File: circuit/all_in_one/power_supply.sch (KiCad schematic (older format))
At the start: 23 parts

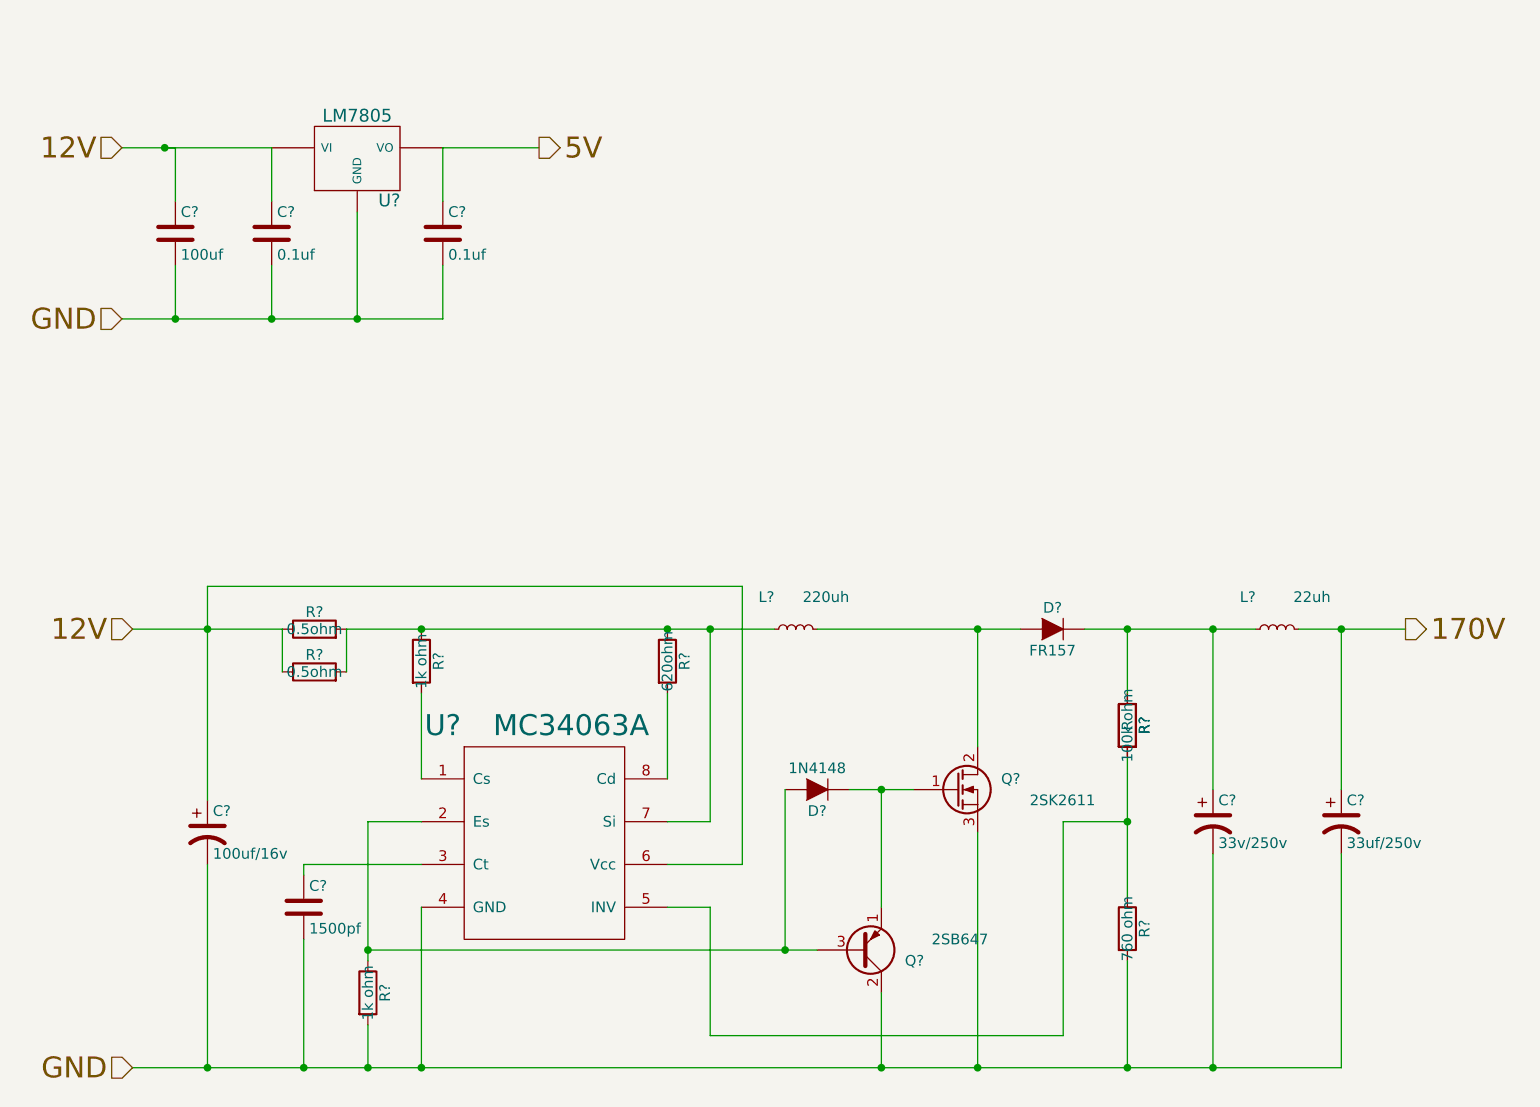
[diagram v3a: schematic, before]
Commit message: [All in one]Define part of compoment's footprint
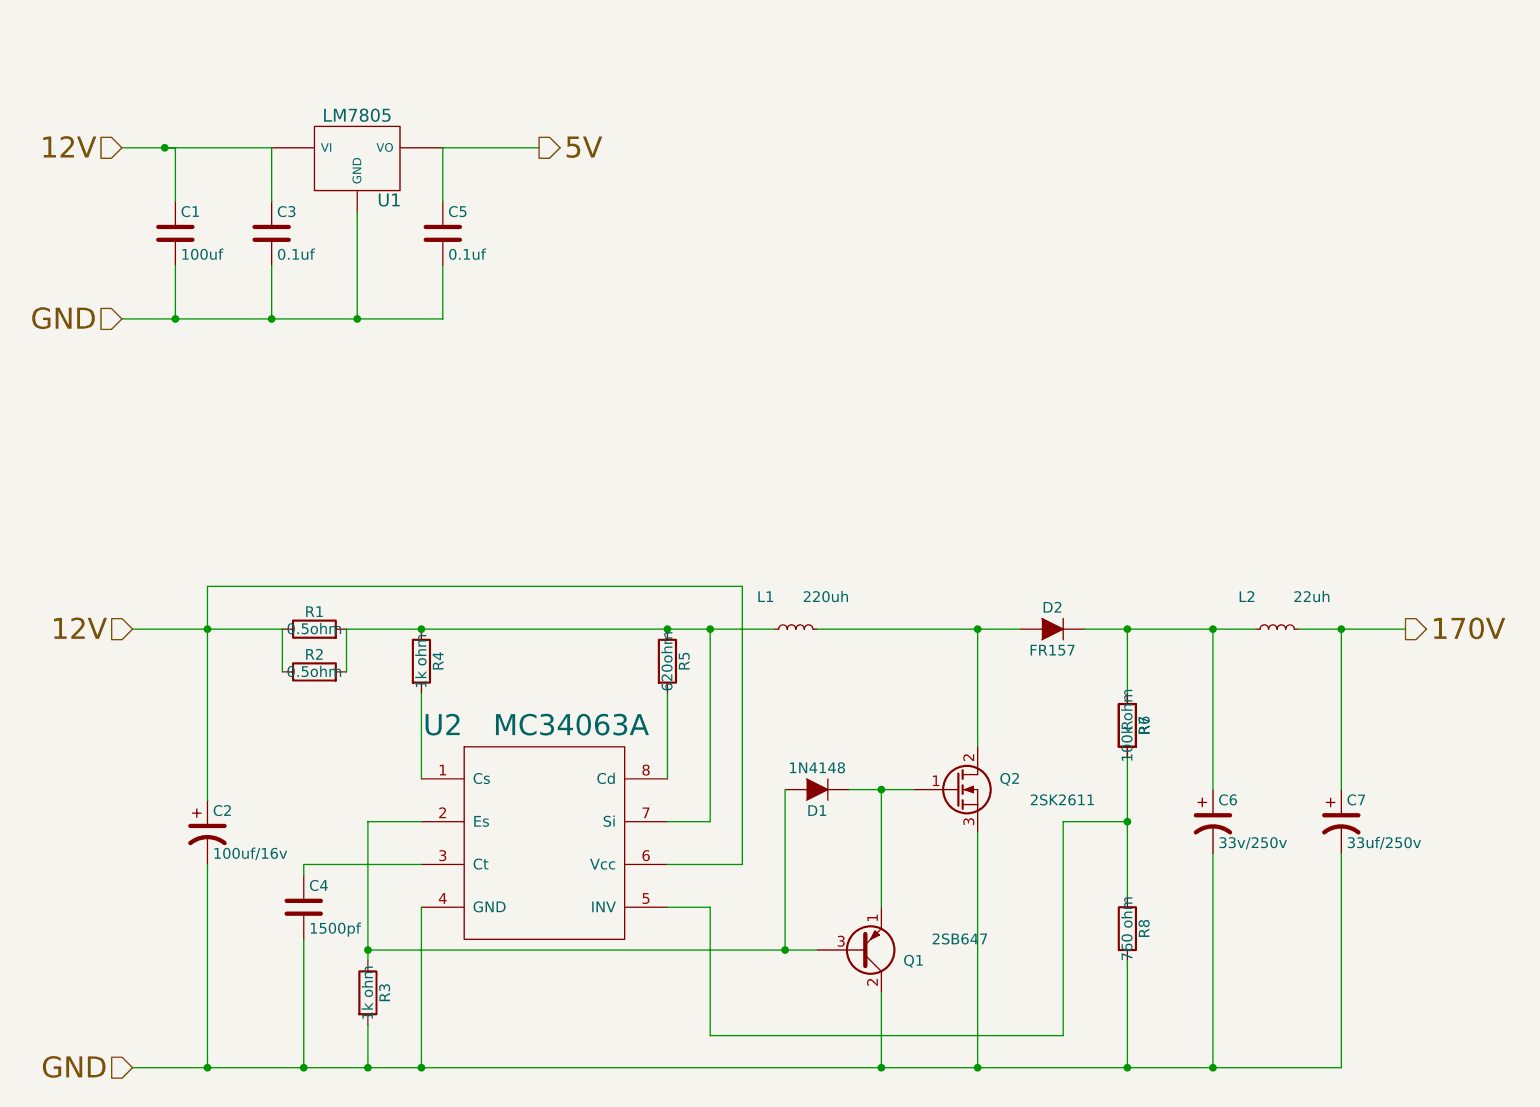
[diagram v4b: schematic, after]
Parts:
- U1: renamed from U?; footprint (none) -> Transistors_SMD:sot404
- U2: renamed from U?; footprint (none) -> Power_Integrations:SO-8
- gave numbers to parts that had none: 21
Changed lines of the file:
@@
 GND
 $Comp
-L LM7805 U?
+L LM7805 U1
 U 1 1 56462C05
 P 3600 1750
-F 0 "U?" H 3750 1554 60  0000 C CNN
+F 0 "U1" H 3750 1554 60  0000 C CNN
 F 1 "LM7805" H 3600 1950 60  0000 C CNN
-F 2 "" H 3600 1750 60  0000 C CNN
+F 2 "Transistors_SMD:sot404" H 3600 1750 60  0001 C CNN
 F 3 "" H 3600 1750 60  0000 C CNN
 	1    3600 1750
@@
 $EndComp
 $Comp
-L C C?
+L C C1
 U 1 1 56462C7B
 P 2750 2100
-F 0 "C?" H 2775 2200 50  0000 L CNN
+F 0 "C1" H 2775 2200 50  0000 L CNN
 F 1 "100uf" H 2775 2000 50  0000 L CNN
-F 2 "" H 2788 1950 30  0000 C CNN
+F 2 "" H 2788 1950 30  0001 C CNN
 F 3 "" H 2750 2100 60  0000 C CNN
 	1    2750 2100
@@
 $EndComp
 $Comp
-L C C?
+L C C3
 U 1 1 56462D16
 P 3200 2100
-F 0 "C?" H 3225 2200 50  0000 L CNN
+F 0 "C3" H 3225 2200 50  0000 L CNN
 F 1 "0.1uf" H 3225 2000 50  0000 L CNN
-F 2 "" H 3238 1950 30  0000 C CNN
+F 2 "" H 3238 1950 30  0001 C CNN
 F 3 "" H 3200 2100 60  0000 C CNN
 	1    3200 2100
@@
 $EndComp
 $Comp
-L C C?
+L C C5
 U 1 1 56462D5B
 P 4000 2100
-F 0 "C?" H 4025 2200 50  0000 L CNN
+F 0 "C5" H 4025 2200 50  0000 L CNN
 F 1 "0.1uf" H 4025 2000 50  0000 L CNN
-F 2 "" H 4038 1950 30  0000 C CNN
+F 2 "" H 4038 1950 30  0001 C CNN
 F 3 "" H 4000 2100 60  0000 C CNN
 	1    4000 2100
@@
 Connection ~ 2700 1700
 $Comp
-L MC34063A U?
+L MC34063A U2
 U 1 1 564633D2
 P 4500 5000
-F 0 "U?" H 4000 5600 98  0000 C CNN
+F 0 "U2" H 4000 5600 98  0000 C CNN
 F 1 "MC34063A" H 4600 5600 98  0000 C CNN
-F 2 "" H 4500 5600 98  0000 C CNN
+F 2 "Power_Integrations:SO-8" H 4500 5600 98  0001 C CNN
 F 3 "" H 4500 5600 98  0000 C CNN
 	1    4500 5000
@@
 $EndComp
 $Comp
-L C C?
+L C C4
 U 1 1 5646359C
 P 3350 5250
-F 0 "C?" H 3375 5350 50  0000 L CNN
+F 0 "C4" H 3375 5350 50  0000 L CNN
 F 1 "1500pf" H 3375 5150 50  0000 L CNN
-F 2 "" H 3388 5100 30  0000 C CNN
+F 2 "" H 3388 5100 30  0001 C CNN
 F 3 "" H 3350 5250 60  0000 C CNN
 	1    3350 5250
@@
 $EndComp
 $Comp
-L R R?
+L R R1
 U 1 1 56463665
 P 3400 3950
-F 0 "R?" V 3480 3950 50  0000 C CNN
+F 0 "R1" V 3480 3950 50  0000 C CNN
 F 1 "0.5ohm" V 3400 3950 50  0000 C CNN
-F 2 "" V 3330 3950 30  0000 C CNN
+F 2 "" V 3330 3950 30  0001 C CNN
 F 3 "" H 3400 3950 30  0000 C CNN
 	1    3400 3950
@@
 $EndComp
 $Comp
-L R R?
+L R R2
 U 1 1 564636F4
 P 3400 4150
-F 0 "R?" V 3480 4150 50  0000 C CNN
+F 0 "R2" V 3480 4150 50  0000 C CNN
 F 1 "0.5ohm" V 3400 4150 50  0000 C CNN
-F 2 "" V 3330 4150 30  0000 C CNN
+F 2 "" V 3330 4150 30  0001 C CNN
 F 3 "" H 3400 4150 30  0000 C CNN
 	1    3400 4150
@@
 $EndComp
 $Comp
-L R R?
+L R R4
 U 1 1 56463737
 P 3900 4100
-F 0 "R?" V 3980 4100 50  0000 C CNN
+F 0 "R4" V 3980 4100 50  0000 C CNN
 F 1 "1k ohm" V 3900 4100 50  0000 C CNN
-F 2 "" V 3830 4100 30  0000 C CNN
+F 2 "" V 3830 4100 30  0001 C CNN
 F 3 "" H 3900 4100 30  0000 C CNN
 	1    3900 4100
@@
 $EndComp
 $Comp
-L R R?
+L R R5
 U 1 1 56463766
 P 5050 4100
-F 0 "R?" V 5130 4100 50  0000 C CNN
+F 0 "R5" V 5130 4100 50  0000 C CNN
 F 1 "620ohm" V 5050 4100 50  0000 C CNN
-F 2 "" V 4980 4100 30  0000 C CNN
+F 2 "" V 4980 4100 30  0001 C CNN
 F 3 "" H 5050 4100 30  0000 C CNN
 	1    5050 4100
@@
 $EndComp
 $Comp
-L CP1 C?
+L CP1 C2
 U 1 1 564637A1
 P 2900 4900
-F 0 "C?" H 2925 5000 50  0000 L CNN
+F 0 "C2" H 2925 5000 50  0000 L CNN
 F 1 "100uf/16v" H 2925 4800 50  0000 L CNN
-F 2 "" H 2900 4900 60  0000 C CNN
+F 2 "" H 2900 4900 60  0001 C CNN
 F 3 "" H 2900 4900 60  0000 C CNN
 	1    2900 4900
@@
 $EndComp
 $Comp
-L CP1 C?
+L CP1 C6
 U 1 1 56463846
 P 7600 4850
-F 0 "C?" H 7625 4950 50  0000 L CNN
+F 0 "C6" H 7625 4950 50  0000 L CNN
 F 1 "33v/250v" H 7625 4750 50  0000 L CNN
-F 2 "" H 7600 4850 60  0000 C CNN
+F 2 "" H 7600 4850 60  0001 C CNN
 F 3 "" H 7600 4850 60  0000 C CNN
 	1    7600 4850
@@
 $EndComp
 $Comp
-L CP1 C?
+L CP1 C7
 U 1 1 5646389B
 P 8200 4850
-F 0 "C?" H 8225 4950 50  0000 L CNN
+F 0 "C7" H 8225 4950 50  0000 L CNN
 F 1 "33uf/250v" H 8225 4750 50  0000 L CNN
-F 2 "" H 8200 4850 60  0000 C CNN
+F 2 "" H 8200 4850 60  0001 C CNN
 F 3 "" H 8200 4850 60  0000 C CNN
 	1    8200 4850
@@
 $EndComp
 $Comp
-L R R?
+L R R6
 U 1 1 56463908
 P 7200 4400
-F 0 "R?" V 7280 4400 50  0000 C CNN
+F 0 "R6" V 7280 4400 50  0000 C CNN
 F 1 "100k ohm" V 7200 4400 50  0000 C CNN
-F 2 "" V 7130 4400 30  0000 C CNN
+F 2 "" V 7130 4400 30  0001 C CNN
 F 3 "" H 7200 4400 30  0000 C CNN
 	1    7200 4400
@@
 $EndComp
 $Comp
-L R R?
+L R R8
 U 1 1 56463951
 P 7200 5350
-F 0 "R?" V 7280 5350 50  0000 C CNN
+F 0 "R8" V 7280 5350 50  0000 C CNN
 F 1 "760 ohm" V 7200 5350 50  0000 C CNN
-F 2 "" V 7130 5350 30  0000 C CNN
+F 2 "" V 7130 5350 30  0001 C CNN
 F 3 "" H 7200 5350 30  0000 C CNN
 	1    7200 5350
@@
 $EndComp
 $Comp
-L D D?
+L D D2
 U 1 1 56463990
 P 6850 3950
-F 0 "D?" H 6850 4050 50  0000 C CNN
+F 0 "D2" H 6850 4050 50  0000 C CNN
 F 1 "FR157" H 6850 3850 50  0000 C CNN
-F 2 "" H 6850 3950 60  0000 C CNN
+F 2 "" H 6850 3950 60  0001 C CNN
 F 3 "" H 6850 3950 60  0000 C CNN
 	1    6850 3950
@@
 $EndComp
 $Comp
-L D D?
+L D D1
 U 1 1 564639E5
 P 5750 4700
-F 0 "D?" H 5750 4800 50  0000 C CNN
+F 0 "D1" H 5750 4800 50  0000 C CNN
 F 1 "1N4148" H 5750 4600 50  0000 C CNN
-F 2 "" H 5750 4700 60  0000 C CNN
+F 2 "" H 5750 4700 60  0001 C CNN
 F 3 "" H 5750 4700 60  0000 C CNN
 	1    5750 4700
@@
 	3900 5250 3900 6000
 $Comp
-L R R?
+L R R3
 U 1 1 5646515D
 P 3650 5650
-F 0 "R?" V 3730 5650 50  0000 C CNN
+F 0 "R3" V 3730 5650 50  0000 C CNN
 F 1 "1k ohm" V 3650 5650 50  0000 C CNN
-F 2 "" V 3580 5650 30  0000 C CNN
+F 2 "" V 3580 5650 30  0001 C CNN
 F 3 "" H 3650 5650 30  0000 C CNN
 	1    3650 5650
@@
 	3350 5050 3900 5050
 $Comp
-L L_Small L?
+L L_Small L1
 U 1 1 564660D5
 P 5650 3950
-F 0 "L?" V 5800 4050 50  0000 L CNN
+F 0 "L1" V 5800 4050 50  0000 L CNN
 F 1 "220uh" V 5800 3700 50  0000 L CNN
-F 2 "" H 5650 3950 60  0000 C CNN
+F 2 "" H 5650 3950 60  0001 C CNN
 F 3 "" H 5650 3950 60  0000 C CNN
 	1    5650 3950
@@
 $EndComp
 $Comp
-L L_Small L?
+L L_Small L2
 U 1 1 56466786
 P 7900 3950
-F 0 "L?" V 8050 4050 50  0000 L CNN
+F 0 "L2" V 8050 4050 50  0000 L CNN
 F 1 "22uh" V 8050 3700 50  0000 L CNN
-F 2 "" H 7900 3950 60  0000 C CNN
+F 2 "" H 7900 3950 60  0001 C CNN
 F 3 "" H 7900 3950 60  0000 C CNN
 	1    7900 3950
@@
 Connection ~ 5250 3950
 $Comp
-L Q_PNP_ECB Q?
+L Q_PNP_ECB Q1
 U 1 1 56466938
 P 5950 5450
-F 0 "Q?" H 6250 5500 50  0000 R CNN
+F 0 "Q1" H 6250 5500 50  0000 R CNN
 F 1 "2SB647" H 6550 5400 50  0000 R CNN
-F 2 "" H 6150 5550 29  0000 C CNN
+F 2 "" H 6150 5550 29  0001 C CNN
 F 3 "" H 5950 5450 60  0000 C CNN
 	1    5950 5450
@@
 $EndComp
 $Comp
-L Q_NMOS_GDS Q?
+L Q_NMOS_GDS Q2
 U 1 1 56466AEF
 P 6400 4700
-F 0 "Q?" H 6700 4750 50  0000 R CNN
+F 0 "Q2" H 6700 4750 50  0000 R CNN
 F 1 "2SK2611" H 7050 4650 50  0000 R CNN
-F 2 "" H 6600 4800 29  0000 C CNN
+F 2 "" H 6600 4800 29  0001 C CNN
 F 3 "" H 6400 4700 60  0000 C CNN
 	1    6400 4700
@@
 Connection ~ 8200 3950
 $Comp
-L R R?
+L R R7
 U 1 1 56481750
 P 7200 4400
-F 0 "R?" V 7280 4400 50  0000 C CNN
+F 0 "R7" V 7280 4400 50  0000 C CNN
 F 1 "R" V 7200 4400 50  0000 C CNN
-F 2 "" V 7130 4400 30  0000 C CNN
+F 2 "" V 7130 4400 30  0001 C CNN
 F 3 "" H 7200 4400 30  0000 C CNN
 	1    7200 4400

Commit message: [All in one]Select resister and power jack's footprint
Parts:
- R1, R2, R3, R4, R5, R6, R7, R8: footprint (none) -> Resistors_SMD:R_0805_HandSoldering
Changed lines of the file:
@@
 F 0 "R1" V 3480 3950 50  0000 C CNN
 F 1 "0.5ohm" V 3400 3950 50  0000 C CNN
-F 2 "" V 3330 3950 30  0001 C CNN
+F 2 "Resistors_SMD:R_0805_HandSoldering" V 3330 3950 30  0001 C CNN
 F 3 "" H 3400 3950 30  0000 C CNN
 	1    3400 3950
@@
 F 0 "R2" V 3480 4150 50  0000 C CNN
 F 1 "0.5ohm" V 3400 4150 50  0000 C CNN
-F 2 "" V 3330 4150 30  0001 C CNN
+F 2 "Resistors_SMD:R_0805_HandSoldering" V 3330 4150 30  0001 C CNN
 F 3 "" H 3400 4150 30  0000 C CNN
 	1    3400 4150
@@
 F 0 "R4" V 3980 4100 50  0000 C CNN
 F 1 "1k ohm" V 3900 4100 50  0000 C CNN
-F 2 "" V 3830 4100 30  0001 C CNN
+F 2 "Resistors_SMD:R_0805_HandSoldering" V 3830 4100 30  0001 C CNN
 F 3 "" H 3900 4100 30  0000 C CNN
 	1    3900 4100
@@
 F 0 "R5" V 5130 4100 50  0000 C CNN
 F 1 "620ohm" V 5050 4100 50  0000 C CNN
-F 2 "" V 4980 4100 30  0001 C CNN
+F 2 "Resistors_SMD:R_0805_HandSoldering" V 4980 4100 30  0001 C CNN
 F 3 "" H 5050 4100 30  0000 C CNN
 	1    5050 4100
@@
 F 0 "R6" V 7280 4400 50  0000 C CNN
 F 1 "100k ohm" V 7200 4400 50  0000 C CNN
-F 2 "" V 7130 4400 30  0001 C CNN
+F 2 "Resistors_SMD:R_0805_HandSoldering" V 7130 4400 30  0001 C CNN
 F 3 "" H 7200 4400 30  0000 C CNN
 	1    7200 4400
@@
 F 0 "R8" V 7280 5350 50  0000 C CNN
 F 1 "760 ohm" V 7200 5350 50  0000 C CNN
-F 2 "" V 7130 5350 30  0001 C CNN
+F 2 "Resistors_SMD:R_0805_HandSoldering" V 7130 5350 30  0001 C CNN
 F 3 "" H 7200 5350 30  0000 C CNN
 	1    7200 5350
@@
 F 0 "R3" V 3730 5650 50  0000 C CNN
 F 1 "1k ohm" V 3650 5650 50  0000 C CNN
-F 2 "" V 3580 5650 30  0001 C CNN
+F 2 "Resistors_SMD:R_0805_HandSoldering" V 3580 5650 30  0001 C CNN
 F 3 "" H 3650 5650 30  0000 C CNN
 	1    3650 5650
@@
 F 0 "R7" V 7280 4400 50  0000 C CNN
 F 1 "R" V 7200 4400 50  0000 C CNN
-F 2 "" V 7130 4400 30  0001 C CNN
+F 2 "Resistors_SMD:R_0805_HandSoldering" V 7130 4400 30  0001 C CNN
 F 3 "" H 7200 4400 30  0000 C CNN
 	1    7200 4400

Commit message: [All in one]Select footprint for capacitors
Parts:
- C1, C2: footprint (none) -> Capacitors_Tantalum_SMD:TantalC_SizeC_EIA-6032_HandSoldering
- C3, C4, C5: footprint (none) -> Capacitors_SMD:C_0805_HandSoldering
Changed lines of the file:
@@
 F 0 "C1" H 2775 2200 50  0000 L CNN
 F 1 "100uf" H 2775 2000 50  0000 L CNN
-F 2 "" H 2788 1950 30  0001 C CNN
+F 2 "Capacitors_Tantalum_SMD:TantalC_SizeC_EIA-6032_HandSoldering" H 2788 1950 30  0001 C CNN
 F 3 "" H 2750 2100 60  0000 C CNN
 	1    2750 2100
@@
 F 0 "C3" H 3225 2200 50  0000 L CNN
 F 1 "0.1uf" H 3225 2000 50  0000 L CNN
-F 2 "" H 3238 1950 30  0001 C CNN
+F 2 "Capacitors_SMD:C_0805_HandSoldering" H 3238 1950 30  0001 C CNN
 F 3 "" H 3200 2100 60  0000 C CNN
 	1    3200 2100
@@
 F 0 "C5" H 4025 2200 50  0000 L CNN
 F 1 "0.1uf" H 4025 2000 50  0000 L CNN
-F 2 "" H 4038 1950 30  0001 C CNN
+F 2 "Capacitors_SMD:C_0805_HandSoldering" H 4038 1950 30  0001 C CNN
 F 3 "" H 4000 2100 60  0000 C CNN
 	1    4000 2100
@@
 F 0 "C4" H 3375 5350 50  0000 L CNN
 F 1 "1500pf" H 3375 5150 50  0000 L CNN
-F 2 "" H 3388 5100 30  0001 C CNN
+F 2 "Capacitors_SMD:C_0805_HandSoldering" H 3388 5100 30  0001 C CNN
 F 3 "" H 3350 5250 60  0000 C CNN
 	1    3350 5250
@@
 F 0 "C2" H 2925 5000 50  0000 L CNN
 F 1 "100uf/16v" H 2925 4800 50  0000 L CNN
-F 2 "" H 2900 4900 60  0001 C CNN
+F 2 "Capacitors_Tantalum_SMD:TantalC_SizeC_EIA-6032_HandSoldering" H 2900 4900 60  0001 C CNN
 F 3 "" H 2900 4900 60  0000 C CNN
 	1    2900 4900

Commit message: Finished select all the component footprint
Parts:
- C6, C7: footprint (none) -> Capacitors_ThroughHole:C_Radial_D13_L21_P5
- D1, D2: footprint (none) -> Diodes_ThroughHole:Diode_DO-35_SOD27_Horizontal_RM10
- L1, L2: footprint (none) -> Inductors:INDUCTOR_V
- Q1: footprint (none) -> TO_SOT_Packages_THT:TO-92_Inline_Narrow_Oval
- Q2: footprint (none) -> TO_SOT_Packages_THT:TO-220_Neutral123_PadsOnly
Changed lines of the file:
@@
 F 0 "C6" H 7625 4950 50  0000 L CNN
 F 1 "33v/250v" H 7625 4750 50  0000 L CNN
-F 2 "" H 7600 4850 60  0001 C CNN
+F 2 "Capacitors_ThroughHole:C_Radial_D13_L21_P5" H 7600 4850 60  0001 C CNN
 F 3 "" H 7600 4850 60  0000 C CNN
 	1    7600 4850
@@
 F 0 "C7" H 8225 4950 50  0000 L CNN
 F 1 "33uf/250v" H 8225 4750 50  0000 L CNN
-F 2 "" H 8200 4850 60  0001 C CNN
+F 2 "Capacitors_ThroughHole:C_Radial_D13_L21_P5" H 8200 4850 60  0001 C CNN
 F 3 "" H 8200 4850 60  0000 C CNN
 	1    8200 4850
@@
 F 0 "D2" H 6850 4050 50  0000 C CNN
 F 1 "FR157" H 6850 3850 50  0000 C CNN
-F 2 "" H 6850 3950 60  0001 C CNN
+F 2 "Diodes_ThroughHole:Diode_DO-35_SOD27_Horizontal_RM10" H 6850 3950 60  0001 C CNN
 F 3 "" H 6850 3950 60  0000 C CNN
 	1    6850 3950
@@
 F 0 "D1" H 5750 4800 50  0000 C CNN
 F 1 "1N4148" H 5750 4600 50  0000 C CNN
-F 2 "" H 5750 4700 60  0001 C CNN
+F 2 "Diodes_ThroughHole:Diode_DO-35_SOD27_Horizontal_RM10" H 5750 4700 60  0001 C CNN
 F 3 "" H 5750 4700 60  0000 C CNN
 	1    5750 4700
@@
 F 0 "L1" V 5800 4050 50  0000 L CNN
 F 1 "220uh" V 5800 3700 50  0000 L CNN
-F 2 "" H 5650 3950 60  0001 C CNN
+F 2 "Inductors:INDUCTOR_V" H 5650 3950 60  0001 C CNN
 F 3 "" H 5650 3950 60  0000 C CNN
 	1    5650 3950
@@
 F 0 "L2" V 8050 4050 50  0000 L CNN
 F 1 "22uh" V 8050 3700 50  0000 L CNN
-F 2 "" H 7900 3950 60  0001 C CNN
+F 2 "Inductors:INDUCTOR_V" H 7900 3950 60  0001 C CNN
 F 3 "" H 7900 3950 60  0000 C CNN
 	1    7900 3950
@@
 F 0 "Q1" H 6250 5500 50  0000 R CNN
 F 1 "2SB647" H 6550 5400 50  0000 R CNN
-F 2 "" H 6150 5550 29  0001 C CNN
+F 2 "TO_SOT_Packages_THT:TO-92_Inline_Narrow_Oval" H 6150 5550 29  0001 C CNN
 F 3 "" H 5950 5450 60  0000 C CNN
 	1    5950 5450
@@
 F 0 "Q2" H 6700 4750 50  0000 R CNN
 F 1 "2SK2611" H 7050 4650 50  0000 R CNN
-F 2 "" H 6600 4800 29  0001 C CNN
+F 2 "TO_SOT_Packages_THT:TO-220_Neutral123_PadsOnly" H 6600 4800 29  0001 C CNN
 F 3 "" H 6400 4700 60  0000 C CNN
 	1    6400 4700
